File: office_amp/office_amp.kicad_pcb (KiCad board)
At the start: 4 copper layers, 120 x 100 mm, 153 parts, among them J1 Jack-DC, J2 Conn_01x03_Female, J3 Conn_02x07_Odd_Even, J7 Screw_Terminal_01x04, J8 Conn_01x03_Female, K1 V23079-A1003-B301, K2 V23079-A1003-B301, K3 V23079-A1003-B301, K4 V23079-A1003-B301, Q1 DMT6012LSS, Q2 BC858, Q3 BC858, Q4 BC850, Q5 BC850, Q6 BC856, Q7 BC850, Q8 BC856, Q9 BC856, U1 LM74700, U10 DS1882E, U11 TL084, U12 TL082, U2 LM7805_TO220, U3 TL082, U4 TBA_2-2421, U5 MH-M18, U6 TPA3123D2, U7 LM7812_TO220, U8 IL300, U9 IL300

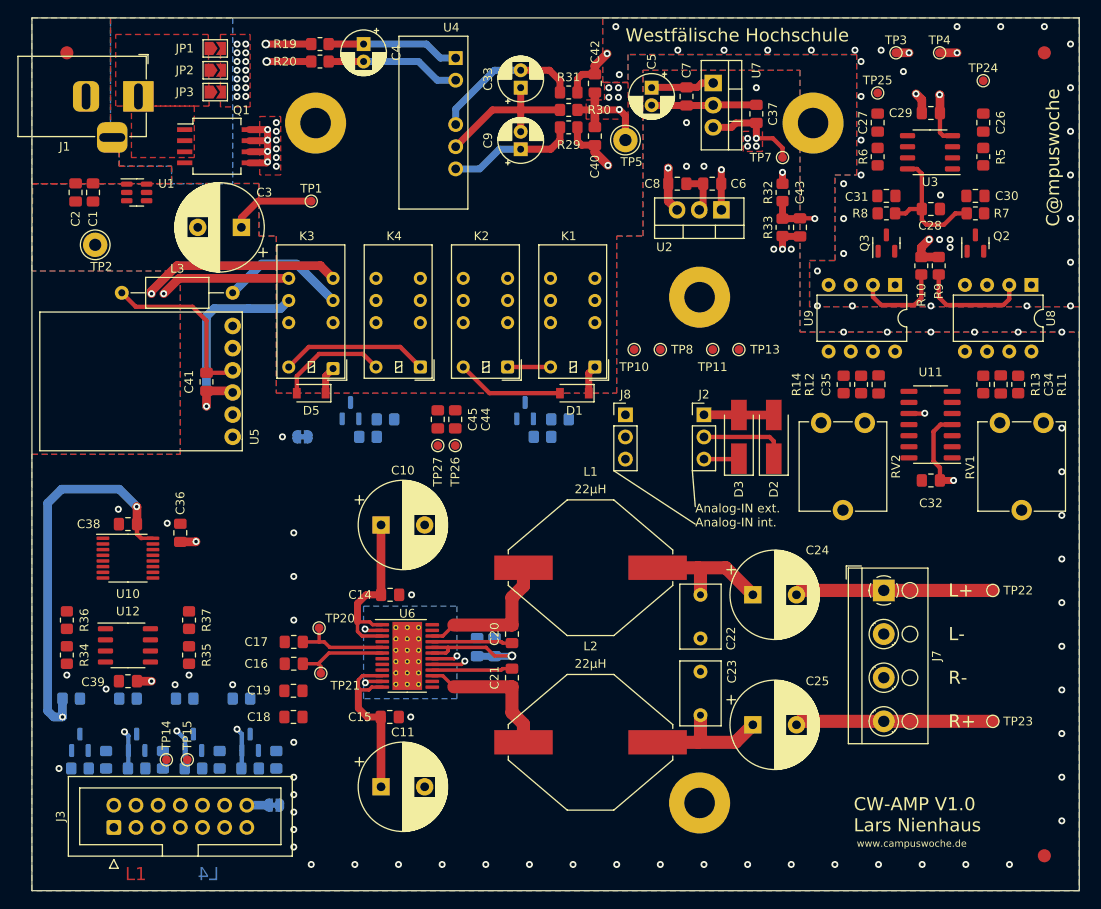
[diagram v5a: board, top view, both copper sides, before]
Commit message: removed errors control board, added interrupt pins controllboard
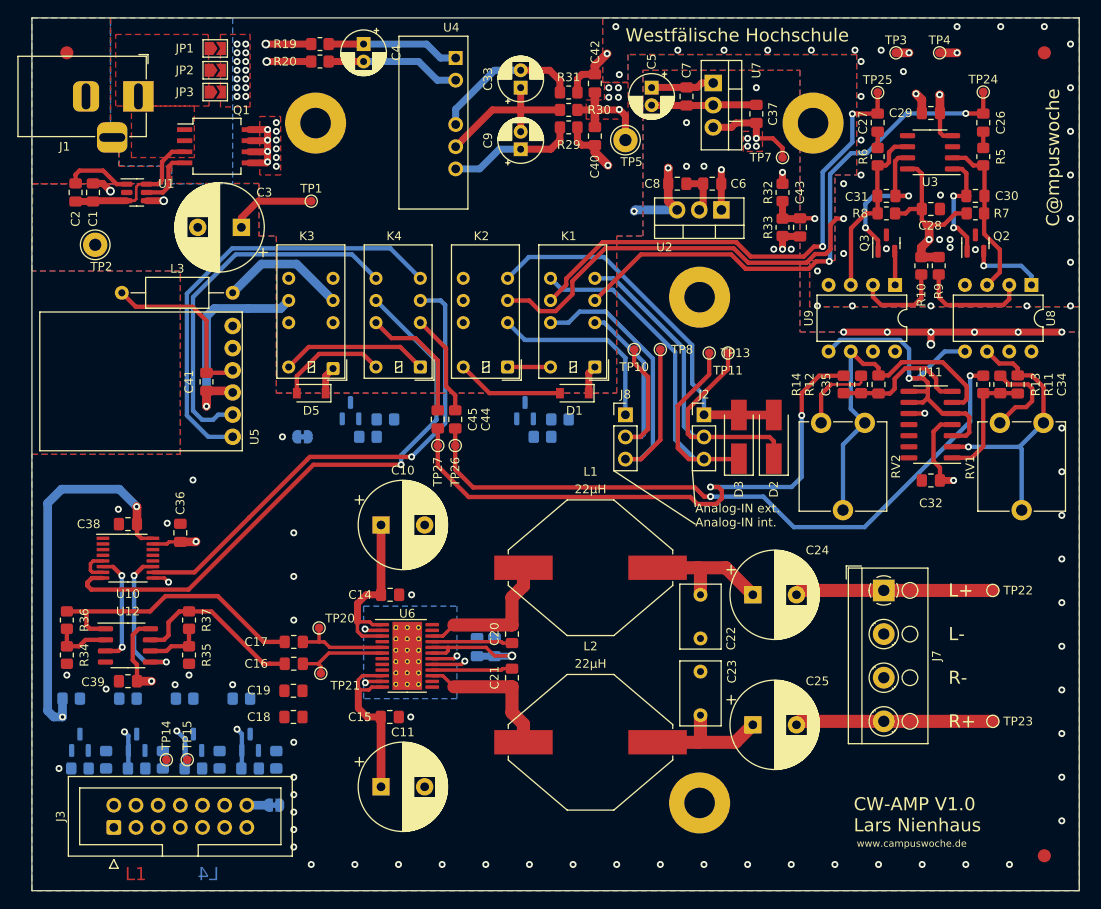
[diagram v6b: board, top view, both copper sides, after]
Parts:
- moved TP13 3.42 mm to (167.6, 96.4)
- moved R11 2.05 mm to (200.9, 100.0)
- moved C34 1.95 mm to (202.9, 100.0)
- moved TP11 1.80 mm to (169.8, 96.4)
- moved TP24 1.30 mm to (199.0, 66.5)
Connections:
- K3 pad 8: GNDD -> GNDREF
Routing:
- net GNDD: track 112.3 -> 20.6 mm, vias 1 -> 0
- net GNDREF: track 188.6 -> 267.4 mm, vias 61 -> 64
- net Net-(C44-Pad2): track 0.00 -> 78.2 mm, vias 0 -> 2
- net /Class_D/L-In: track 0.00 -> 67.8 mm, vias 0 -> 1
- net Net-(C45-Pad2): track 0.00 -> 67.5 mm, vias 0 -> 2
- net /Audio_Isolation/R-In-ISO: track 0.00 -> 63.0 mm, vias 0 -> 2
- net /Audio_Isolation/L-In-ISO: track 0.00 -> 57.5 mm, vias 0 -> 2
- net /Class_D/R-In: track 0.00 -> 57.2 mm, vias 0 -> 1
- net R-In-BT: track 0.00 -> 50.5 mm
- net L-In-An: track 4.02 -> 52.0 mm
- net GND_Input: track 75.6 -> 122.9 mm, vias 41 -> 43
- net L-In-USB: track 0.00 -> 43.6 mm
- net L-In-BT: track 0.00 -> 42.4 mm
- net Net-(C35-Pad2): track 0.00 -> 39.9 mm
- net Net-(U11-Pad3): track 0.00 -> 39.5 mm, vias 0 -> 1
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
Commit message: error correction aftertest; corrected pinout touch; added level shifter for i2c poti; corrected voltages i2c poti
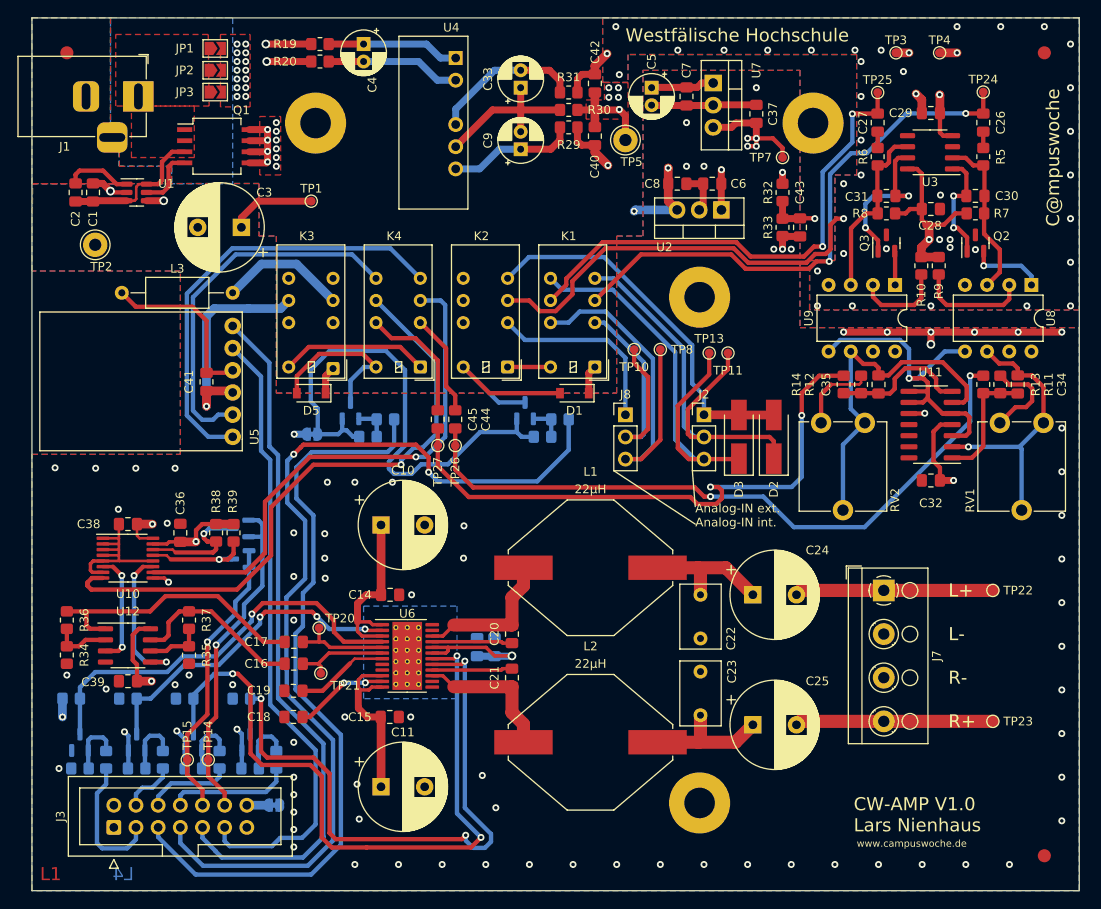
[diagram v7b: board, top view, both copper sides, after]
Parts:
- added Q10: BSS138, Package_TO_SOT_SMD:SOT-23, B.Cu at (113.9, 116.5)
- added Q11: BSS138, Package_TO_SOT_SMD:SOT-23, B.Cu at (113.9, 120.0)
- added R38: 10k, Resistor_SMD:R_0805_2012Metric_Pad1.20x1.40mm_HandSolder, F.Cu at (111.1, 117.0)
- added R39: 10k, Resistor_SMD:R_0805_2012Metric_Pad1.20x1.40mm_HandSolder, F.Cu at (113.1, 117.0)
- moved TP14 4.80 mm to (110.2, 143.0)
- moved STAR5 1.14 mm to (122.1, 105.7)
- turned R21 to 90 degrees
- turned R25 to 90 degrees
- turned R26 to 90 degrees
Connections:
- C38 pad 1: +3V3 -> +5V
- U10 pad 13: /Class_D/SDA -> /Class_D/SDA-5
- U10 pad 14: /Class_D/SCL -> /Class_D/SCL-5
- U10 pad 16: +3V3 -> +5V
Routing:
- net SELECT-Analog: track 0.00 -> 109.8 mm, vias 0 -> 2
- net SELECT-BT: track 0.00 -> 87.5 mm
- net BT-KEY: track 0.00 -> 79.8 mm
- net /Class_D/GAIN0: track 2.97 -> 80.7 mm, vias 1 -> 3
- net BT-MUTE: track 0.00 -> 71.8 mm
- net /Class_D/GAIN1: track 3.89 -> 73.1 mm, vias 1 -> 3
- net GND2: track 0.00 -> 59.5 mm
- net /Class_D/MUTE: track 0.00 -> 47.1 mm, vias 0 -> 1
- net +3V3: track 113.6 -> 71.0 mm, vias 5 -> 4
- net /Class_D/SCL: track 0.00 -> 38.9 mm, vias 0 -> 1
- net /Class_D/~{SD}: track 2.03 -> 37.6 mm, vias 1 -> 3
- net /Class_D/SDA: track 0.00 -> 32.8 mm, vias 0 -> 1
- net GNDREF: track 267.4 -> 288.0 mm, vias 64 -> 81
- net /Class_D/~{AMP-Mute}: track 0.00 -> 15.5 mm
- net /Class_D/AMP-GAIN1: track 0.00 -> 14.3 mm
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- removed copper zone on F.Cu, net +12V
